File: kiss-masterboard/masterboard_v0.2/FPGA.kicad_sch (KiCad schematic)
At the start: 89 parts, among them J10 CRESET, J11 Jumper, J12 Jumper, J13 Conn_02x08_Odd_Even, J14 Conn_02x08_Odd_Even, J15 jmp, J16 jmp, J8 Jumper, U11 TLV75733PDBV, U13 SN74LVC8T245, U14 W25Q, U17 12MHz, U2 SN74LVC8T245, U4 ICE40UP5k-SG48, U5 SN74LVC8T245, U8 TLV75709PDBV

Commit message: adjust c numbers and footprint for hab75
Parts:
- C10: JLCNR C19702 -> (none); LCSC Part # (none) -> C19702
- C11, C12, C15, C16, C19, C24, C25, C28, C29, C30, C31, C57, C61, C9: JLCNR C1525 -> (none); LCSC Part # (none) -> C1525
- C13, C22: JLCNR C15195 -> (none); LCSC Part # (none) -> C15195
- C14, C17, C8: JLCNR C52923 -> (none); LCSC Part # (none) -> C52923
- C18, C23, C26, C54: JLCNR C19666 -> (none); LCSC Part # (none) -> C19666
- C56: JLCNR C14663 -> (none); LCSC Part # (none) -> C14663
- D4: JLCNR C7502714 -> (none); LCSC Part # (none) -> C7502714
- D5: JLCNR C2290 -> (none); LCSC Part # (none) -> C2290
- D6: JLCNR C2286 -> (none); LCSC Part # (none) -> C2286
- J13, J14: JLCNR C32713288 -> (none); LCSC Part # (none) -> C2843216
- R14: JLCNR C25076 -> (none); LCSC Part # (none) -> C25076
- R15, R16, R17, R21, R22, R23, R26, R27, R30: JLCNR C25744 -> (none); LCSC Part # (none) -> C25744
- R20: JLCNR C25104 -> (none); LCSC Part # (none) -> C25104
- R24: JLCNR C25879 -> (none); LCSC Part # (none) -> C25879
- R45, R46, R47, R48: JLCNR C25804 -> (none); LCSC Part # (none) -> C25804
- R51, R52, R53, R54, R55, R56, R57, R58, R59, R60, R61, R62, R63, R64, R65, R66, R67, R68, R69, R70, R71, R72, R73, R74, R75, R76, R77, R78: JLCNR C138015 -> (none); LCSC Part # (none) -> C138015
- U11: JLCNR C485517 -> (none); LCSC Part # (none) -> C485517
- U13, U2, U5: JLCNR C27643 -> (none); LCSC Part # (none) -> C27643
- U4: JLCNR C2678152 -> (none); LCSC Part # (none) -> C2678152
- U8: JLCNR C58464 -> (none); LCSC Part # (none) -> C58464

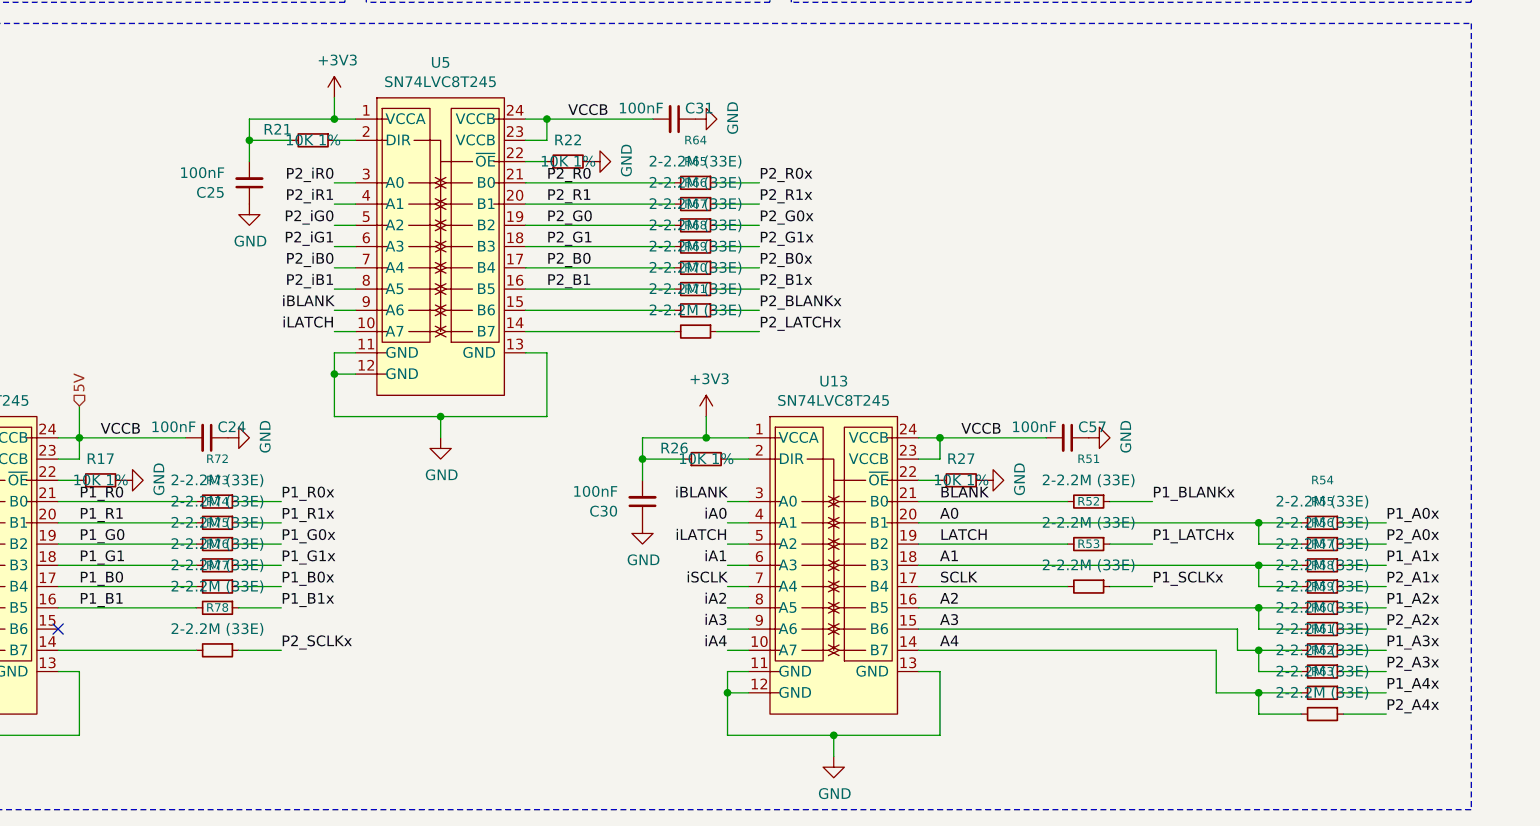
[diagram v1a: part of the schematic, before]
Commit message: replace 2.2mohm with 33ohm for all hub75
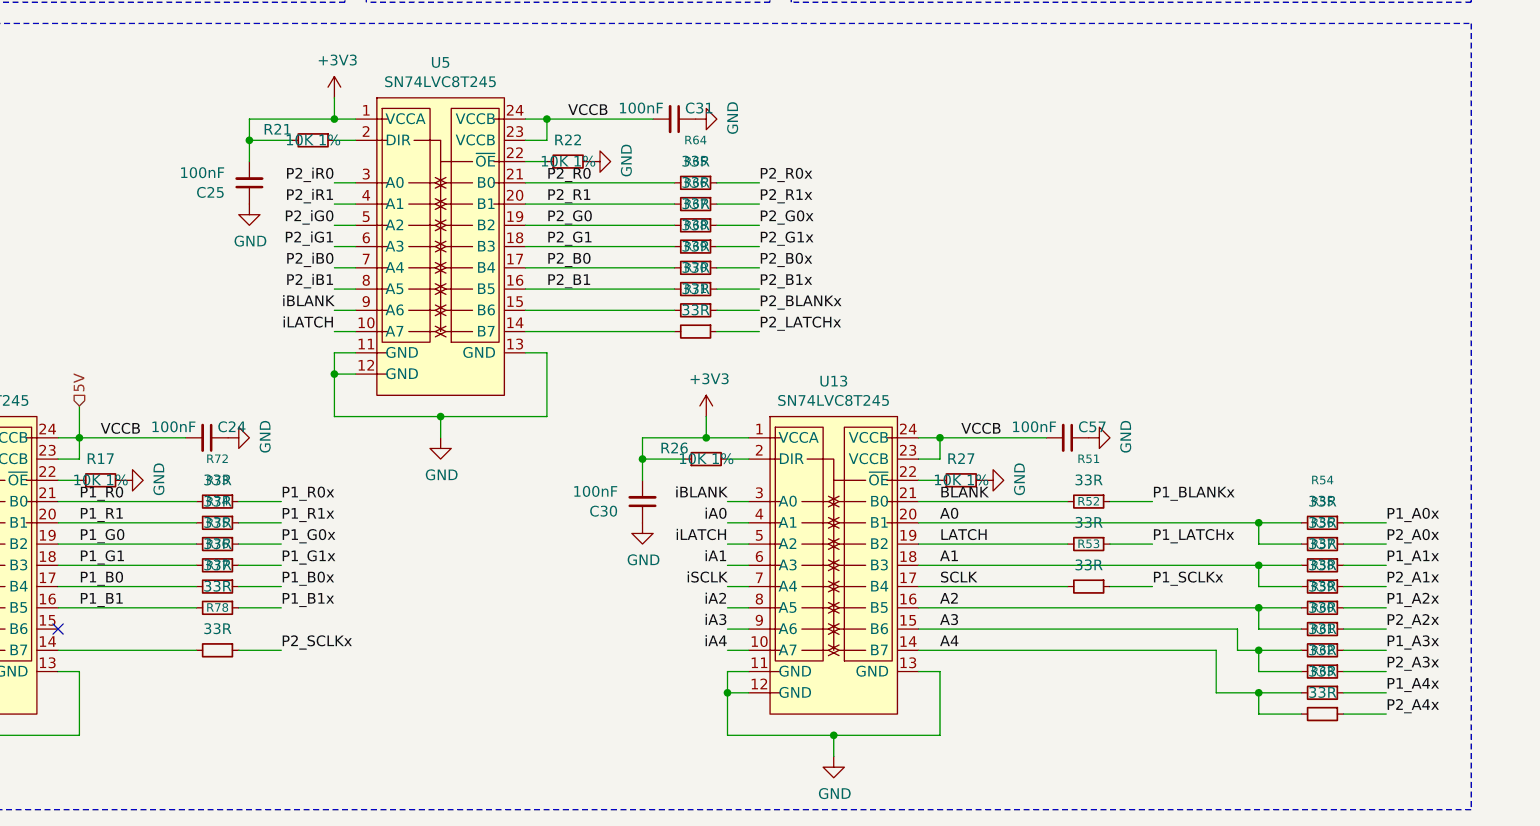
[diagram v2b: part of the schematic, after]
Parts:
- R51, R52, R53, R54, R55, R56, R57, R58, R59, R60, R61, R62, R63, R64, R65, R66, R67, R68, R69, R70, R71, R72, R73, R74, R75, R76, R77, R78: value 2-2.2M (33E) -> 33R; LCSC Part # C138015 -> C25105
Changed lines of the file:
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@@
 			)
 		)
-		(property "Value" "2-2.2M (33E)"
+		(property "Value" "33R"
 			(at 209.55 262.89 90)
 			(show_name no)
@@
 			)
 		)
-		(property "LCSC Part #" "C138015"
+		(property "LCSC Part #" "C25105"
 			(at 209.55 265.43 90)
 			(hide yes)
@@
 			)
 		)
-		(property "Value" "2-2.2M (33E)"
+		(property "Value" "33R"
 			(at 134.62 217.17 90)
 			(show_name no)
@@
 			)
 		)
-		(property "LCSC Part #" "C138015"
+		(property "LCSC Part #" "C25105"
 			(at 134.62 219.71 90)
 			(hide yes)
@@
 			)
 		)
-		(property "Value" "2-2.2M (33E)"
+		(property "Value" "33R"
 			(at 181.61 242.57 90)
 			(show_name no)
@@
 			)
 		)
-		(property "LCSC Part #" "C138015"
+		(property "LCSC Part #" "C25105"
 			(at 181.61 245.11 90)
 			(hide yes)
@@
 			)
 		)
-		(property "Value" "2-2.2M (33E)"
+		(property "Value" "33R"
 			(at 77.47 252.73 90)
 			(show_name no)
@@
 			)
 		)
-		(property "LCSC Part #" "C138015"
+		(property "LCSC Part #" "C25105"
 			(at 77.47 255.27 90)
 			(hide yes)
@@
 			)
 		)
-		(property "Value" "2-2.2M (33E)"
+		(property "Value" "33R"
 			(at 209.55 247.65 90)
 			(show_name no)
@@
 			)
 		)
-		(property "LCSC Part #" "C138015"
+		(property "LCSC Part #" "C25105"
 			(at 209.55 250.19 90)
 			(hide yes)
@@
 			)
 		)
-		(property "Value" "2-2.2M (33E)"
+		(property "Value" "33R"
 			(at 209.55 265.43 90)
 			(show_name no)
@@
 			)
 		)
-		(property "LCSC Part #" "C138015"
+		(property "LCSC Part #" "C25105"
 			(at 209.55 267.97 90)
 			(hide yes)
@@
 			)
 		)
-		(property "Value" "2-2.2M (33E)"
+		(property "Value" "33R"
 			(at 77.47 255.27 90)
 			(show_name no)
@@
 			)
 		)
-		(property "LCSC Part #" "C138015"
+		(property "LCSC Part #" "C25105"
 			(at 77.47 257.81 90)
 			(hide yes)
@@
 			)
 		)
-		(property "Value" "2-2.2M (33E)"
+		(property "Value" "33R"
 			(at 134.62 222.25 90)
 			(show_name no)
@@
 			)
 		)
-		(property "LCSC Part #" "C138015"
+		(property "LCSC Part #" "C25105"
 			(at 134.62 224.79 90)
 			(hide yes)
@@
 			)
 		)
-		(property "Value" "2-2.2M (33E)"
+		(property "Value" "33R"
 			(at 77.47 247.65 90)
 			(show_name no)
@@
 			)
 		)
-		(property "LCSC Part #" "C138015"
+		(property "LCSC Part #" "C25105"
 			(at 77.47 250.19 90)
 			(hide yes)
@@
 			)
 		)
-		(property "Value" "2-2.2M (33E)"
+		(property "Value" "33R"
 			(at 209.55 267.97 90)
 			(show_name no)
@@
 			)
 		)
-		(property "LCSC Part #" "C138015"
+		(property "LCSC Part #" "C25105"
 			(at 209.55 270.51 90)
 			(hide yes)
@@
 			)
 		)
-		(property "Value" "2-2.2M (33E)"
+		(property "Value" "33R"
 			(at 134.62 209.55 90)
 			(show_name no)
@@
 			)
 		)
-		(property "LCSC Part #" "C138015"
+		(property "LCSC Part #" "C25105"
 			(at 134.62 212.09 90)
 			(hide yes)
@@
 			)
 		)
-		(property "Value" "2-2.2M (33E)"
+		(property "Value" "33R"
 			(at 134.62 214.63 90)
 			(show_name no)
@@
 			)
 		)
-		(property "LCSC Part #" "C138015"
+		(property "LCSC Part #" "C25105"
 			(at 134.62 217.17 90)
 			(hide yes)
@@
 			)
 		)
-		(property "Value" "2-2.2M (33E)"
+		(property "Value" "33R"
 			(at 134.62 212.09 90)
 			(show_name no)
@@
 			)
 		)
-		(property "LCSC Part #" "C138015"
+		(property "LCSC Part #" "C25105"
 			(at 134.62 214.63 90)
 			(hide yes)
@@
 			)
 		)
-		(property "Value" "2-2.2M (33E)"
+		(property "Value" "33R"
 			(at 209.55 257.81 90)
 			(show_name no)
@@
 			)
 		)
-		(property "LCSC Part #" "C138015"
+		(property "LCSC Part #" "C25105"
 			(at 209.55 260.35 90)
 			(hide yes)
@@
 			)
 		)
-		(property "Value" "2-2.2M (33E)"
+		(property "Value" "33R"
 			(at 134.62 219.71 90)
 			(show_name no)
@@
 			)
 		)
-		(property "LCSC Part #" "C138015"
+		(property "LCSC Part #" "C25105"
 			(at 134.62 222.25 90)
 			(hide yes)
@@
 			)
 		)
-		(property "Value" "2-2.2M (33E)"
+		(property "Value" "33R"
 			(at 209.55 250.19 90)
 			(show_name no)
@@
 			)
 		)
-		(property "LCSC Part #" "C138015"
+		(property "LCSC Part #" "C25105"
 			(at 209.55 252.73 90)
 			(hide yes)
@@
 			)
 		)
-		(property "Value" "2-2.2M (33E)"
+		(property "Value" "33R"
 			(at 77.47 260.35 90)
 			(show_name no)
@@
 			)
 		)
-		(property "LCSC Part #" "C138015"
+		(property "LCSC Part #" "C25105"
 			(at 77.47 262.89 90)
 			(hide yes)
@@
 			)
 		)
-		(property "Value" "2-2.2M (33E)"
+		(property "Value" "33R"
 			(at 209.55 245.11 90)
 			(show_name no)
@@
 			)
 		)
-		(property "LCSC Part #" "C138015"
+		(property "LCSC Part #" "C25105"
 			(at 209.55 247.65 90)
 			(hide yes)
@@
 			)
 		)
-		(property "Value" "2-2.2M (33E)"
+		(property "Value" "33R"
 			(at 77.47 250.19 90)
 			(show_name no)
@@
 			)
 		)
-		(property "LCSC Part #" "C138015"
+		(property "LCSC Part #" "C25105"
 			(at 77.47 252.73 90)
 			(hide yes)
@@
 			)
 		)
-		(property "Value" "2-2.2M (33E)"
+		(property "Value" "33R"
 			(at 209.55 255.27 90)
 			(show_name no)
@@
 			)
 		)
-		(property "LCSC Part #" "C138015"
+		(property "LCSC Part #" "C25105"
 			(at 209.55 257.81 90)
 			(hide yes)
@@
 			)
 		)
-		(property "Value" "2-2.2M (33E)"
+		(property "Value" "33R"
 			(at 134.62 204.47 90)
 			(show_name no)
@@
 			)
 		)
-		(property "LCSC Part #" "C138015"
+		(property "LCSC Part #" "C25105"
 			(at 134.62 207.01 90)
 			(hide yes)
@@
 			)
 		)
-		(property "Value" "2-2.2M (33E)"
+		(property "Value" "33R"
 			(at 209.55 260.35 90)
 			(show_name no)
@@
 			)
 		)
-		(property "LCSC Part #" "C138015"
+		(property "LCSC Part #" "C25105"
 			(at 209.55 262.89 90)
 			(hide yes)
@@
 			)
 		)
-		(property "Value" "2-2.2M (33E)"
+		(property "Value" "33R"
 			(at 209.55 252.73 90)
 			(show_name no)
@@
 			)
 		)
-		(property "LCSC Part #" "C138015"
+		(property "LCSC Part #" "C25105"
 			(at 209.55 255.27 90)
 			(hide yes)
@@
 			)
 		)
-		(property "Value" "2-2.2M (33E)"
+		(property "Value" "33R"
 			(at 77.47 242.57 90)
 			(show_name no)
@@
 			)
 		)
-		(property "LCSC Part #" "C138015"
+		(property "LCSC Part #" "C25105"
 			(at 77.47 245.11 90)
 			(hide yes)
@@
 			)
 		)
-		(property "Value" "2-2.2M (33E)"
+		(property "Value" "33R"
 			(at 181.61 252.73 90)
 			(show_name no)
@@
 			)
 		)
-		(property "LCSC Part #" "C138015"
+		(property "LCSC Part #" "C25105"
 			(at 181.61 255.27 90)
 			(hide yes)
@@
 			)
 		)
-		(property "Value" "2-2.2M (33E)"
+		(property "Value" "33R"
 			(at 77.47 245.11 90)
 			(show_name no)
@@
 			)
 		)
-		(property "LCSC Part #" "C138015"
+		(property "LCSC Part #" "C25105"
 			(at 77.47 247.65 90)
 			(hide yes)
@@
 			)
 		)
-		(property "Value" "2-2.2M (33E)"
+		(property "Value" "33R"
 			(at 134.62 207.01 90)
 			(show_name no)
@@
 			)
 		)
-		(property "LCSC Part #" "C138015"
+		(property "LCSC Part #" "C25105"
 			(at 134.62 209.55 90)
 			(hide yes)
@@
 			)
 		)
-		(property "Value" "2-2.2M (33E)"
+		(property "Value" "33R"
 			(at 181.61 247.65 90)
 			(show_name no)
@@
 			)
 		)
-		(property "LCSC Part #" "C138015"
+		(property "LCSC Part #" "C25105"
 			(at 181.61 250.19 90)
 			(hide yes)
